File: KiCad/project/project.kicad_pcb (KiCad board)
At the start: 4 copper layers, 50 x 50 mm, 31 parts, among them P1 TerminalBlock 5P 5.0mm, U1 DRV8313PWPR

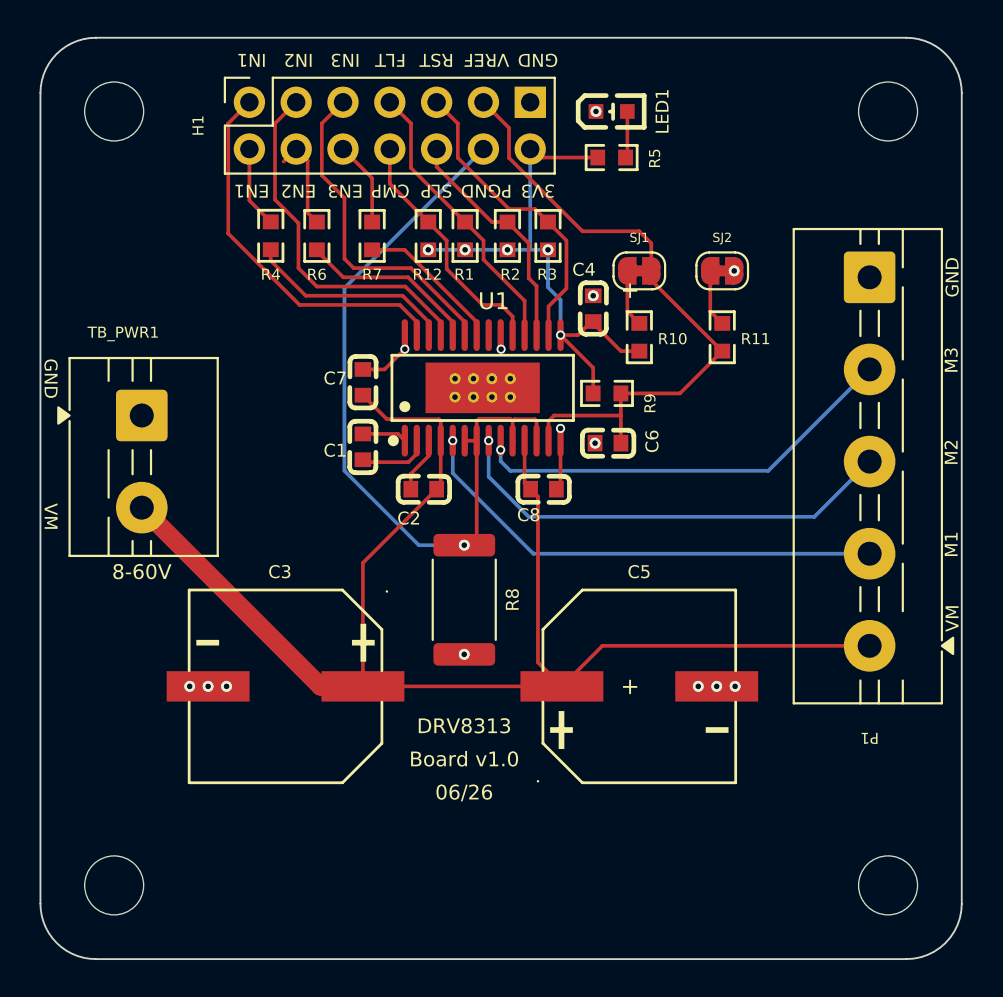
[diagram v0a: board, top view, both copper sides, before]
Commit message: Review manual layout; add power/GND/thermal improvements
Schematic: graphical-only relayout (R8/PGND-label moved, redundant GND
symbol added) — netlist verified byte-identical to prior commit; ERC 101->98.

PCB fixes & improvements:
- Re-ground U1's 8 EP thermal vias (Update-from-Schematic had stripped GND)
  and rename them to pad "29" so they survive every future sync.
- Add Power net class (0.6mm) for VCC/M1/M2/M3/PGND; widen the current-
  carrying runs 0.2->0.6mm with neck-down kept at the HTSSOP escape.
- Add F.Cu + B.Cu GND pours + 38 stitching vias (datasheet 10.1; lowers
  RthJA, better return paths/EMI).
- Extend EP thermal-via array 8->12 (6x2); add GND-return vias at the C7/C8
  VM decoupling caps.

Tooling/docs:
- check_design.py: gate hard on kicad-cli (authoritative for connectivity/
  clearance/shorts); demote KiCadRoutingTools checks to advisory (they false-
  positive on through-pad/off-anchor manual routing); re-baseline ERC to 98.
- Update CLAUDE.md + tools/README.md to match.

Verified: 0 error-severity DRC, 0 unconnected (kicad-cli), check_design PASS.
Manufacturing outputs (manufacturing/, images/) NOT regenerated — still stale.

Co-Authored-By: Claude Opus 4.8 (1M context) <noreply@anthropic.com>
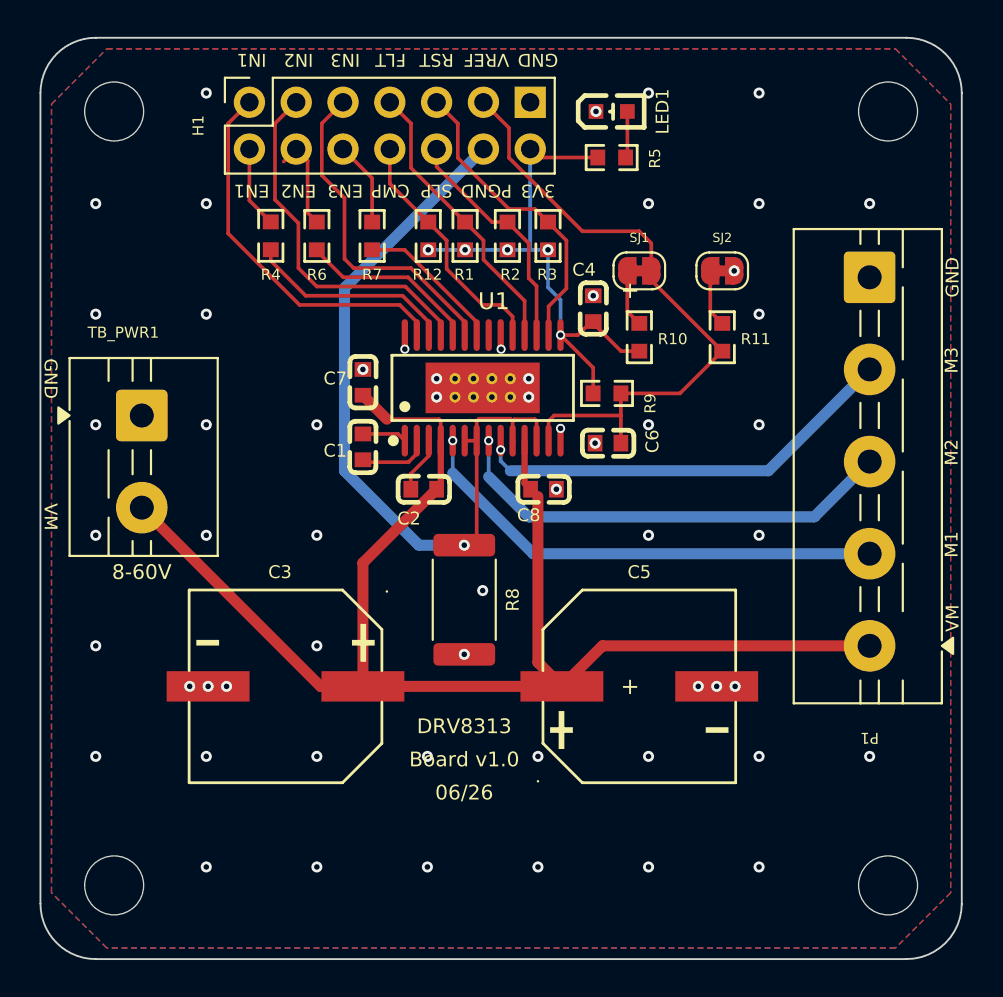
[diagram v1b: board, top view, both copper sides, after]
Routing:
- net GND: track 6.21 -> 1.07 mm, vias 14 -> 58
- added copper zone on B.Cu, net GND
- added copper zone on F.Cu, net GND

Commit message: Enlarge board to 50x50; regenerate fab outputs + square renders
User hand-enlarged the PCB to a full 50x50 mm. Regenerated gerbers, drill,
STEP, and images from the updated board (BOM/CPL unchanged -- no parts moved).

Render canvas was aspect-matched to the old 50x45 board (1600x1440); updated
build_manufacturing.py to 1600x1600 for the now-square board and re-rendered.

Updated CLAUDE.md size references to 50x50 (Goal & status as-built size + dated
note; forward pointer on the superseded 50x45 log entry; render-canvas note).
README spec already updated to 50x50 by the user.

Co-Authored-By: Claude Opus 4.8 (1M context) <noreply@anthropic.com>
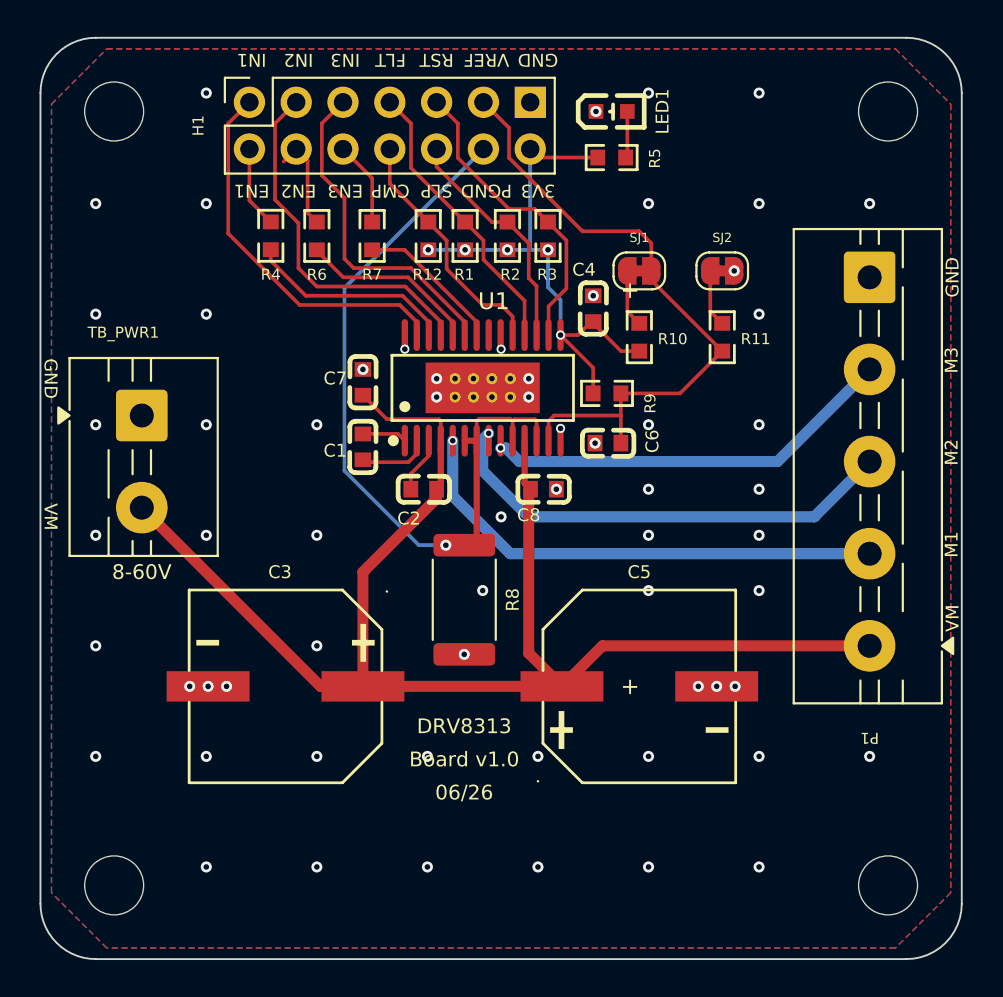
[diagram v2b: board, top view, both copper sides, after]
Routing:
- net M3: track 24.3 -> 22.6 mm
- net PGND: track 42.1 -> 41.1 mm
- net M1: track 27.0 -> 27.7 mm
- net M2: track 24.8 -> 25.4 mm
- net GND: vias 58 -> 63
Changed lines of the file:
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@@
+	)
+	(via
+		(at 173 118)
+		(size 0.6)
+		(drill 0.3)
+		(layers "F.Cu" "B.Cu")
+		(net "GND")
 	)
 	(via
@@
 	)
 	(via
+		(at 159 114)
+		(size 0.6)
+		(drill 0.3)
+		(layers "F.Cu" "B.Cu")
+		(net "GND")
+	)
+	(via
 		(at 173 115)
 		(size 0.6)
@@
 	)
 	(via
+		(at 167 112.5)
+		(size 0.6)
+		(drill 0.3)
+		(layers "F.Cu" "B.Cu")
+		(net "GND")
+	)
+	(via
 		(at 170.7 123.2)
 		(size 0.6)
@@
 	)
 	(via
+		(at 167 118)
+		(size 0.6)
+		(drill 0.3)
+		(layers "F.Cu" "B.Cu")
+		(net "GND")
+	)
+	(via
 		(at 143 115)
 		(size 0.6)
@@
 	(via
 		(at 169.7 123.2)
+		(size 0.6)
+		(drill 0.3)
+		(layers "F.Cu" "B.Cu")
+		(net "GND")
+	)
+	(via
+		(at 173 112.5)
 		(size 0.6)
 		(drill 0.3)
@@
 	)
 	(segment
-		(start 155.5 112.5)
-		(end 151.5 116.5)
-		(width 0.6)
+		(start 160.5 121.4)
+		(end 162.3 123.2)
+		(width 0.6)
+		(layer "F.Cu")
+		(net "VCC")
+	)
+	(segment
+		(start 160.6 112.5)
+		(end 160.2751 112.1751)
+		(width 0.34)
 		(layer "F.Cu")
 		(net "VCC")
@@
 	)
 	(segment
-		(start 161 112.9)
-		(end 161 121.9)
-		(width 0.6)
-		(layer "F.Cu")
-		(net "VCC")
-	)
-	(segment
-		(start 161 121.9)
+		(start 155.5 113)
+		(end 151.5 117)
+		(width 0.6)
+		(layer "F.Cu")
+		(net "VCC")
+	)
+	(segment
+		(start 160.6 112.5)
+		(end 160.5 112.6)
+		(width 0.6)
+		(layer "F.Cu")
+		(net "VCC")
+	)
+	(segment
+		(start 151.5 117)
+		(end 151.5 123.2)
+		(width 0.6)
+		(layer "F.Cu")
+		(net "VCC")
+	)
+	(segment
+		(start 155.5 112.5)
+		(end 155.5 113)
+		(width 0.6)
+		(layer "F.Cu")
+		(net "VCC")
+	)
+	(segment
+		(start 160.5 112.6)
+		(end 160.5 121.4)
+		(width 0.6)
+		(layer "F.Cu")
+		(net "VCC")
+	)
+	(segment
+		(start 164.5 121)
+		(end 179 121)
+		(width 0.6)
+		(layer "F.Cu")
+		(net "VCC")
+	)
+	(segment
+		(start 155.6249 108.70015)
+		(end 155.7249 108.80015)
+		(width 0.2)
+		(layer "F.Cu")
+		(net "VCC")
+	)
+	(segment
+		(start 155.7249 109.8659)
+		(end 155.7249 112.2751)
+		(width 0.34)
+		(layer "F.Cu")
+		(net "VCC")
+	)
+	(segment
+		(start 155.7249 112.2751)
+		(end 155.5 112.5)
+		(width 0.2)
+		(layer "F.Cu")
+		(net "VCC")
+	)
+	(segment
+		(start 162.3 123.2)
+		(end 164.5 121)
+		(width 0.6)
+		(layer "F.Cu")
+		(net "VCC")
+	)
+	(segment
+		(start 160.2751 109.8659)
+		(end 160.3 109.85)
+		(width 0.2)
+		(layer "F.Cu")
+		(net "VCC")
+	)
+	(segment
+		(start 151.5 123.2)
 		(end 162.3 123.2)
 		(width 0.6)
@@
 	)
 	(segment
-		(start 160.6 112.5)
-		(end 160.2751 112.1751)
-		(width 0.34)
-		(layer "F.Cu")
-		(net "VCC")
-	)
-	(segment
-		(start 164.5 121)
-		(end 179 121)
-		(width 0.6)
-		(layer "F.Cu")
-		(net "VCC")
-	)
-	(segment
-		(start 151.5 116.5)
-		(end 151.5 123.2)
-		(width 0.6)
-		(layer "F.Cu")
-		(net "VCC")
-	)
-	(segment
-		(start 155.6249 108.70015)
-		(end 155.7249 108.80015)
-		(width 0.2)
-		(layer "F.Cu")
-		(net "VCC")
-	)
-	(segment
-		(start 155.7249 109.8659)
-		(end 155.7249 112.2751)
-		(width 0.34)
-		(layer "F.Cu")
-		(net "VCC")
-	)
-	(segment
-		(start 155.7249 112.2751)
-		(end 155.5 112.5)
-		(width 0.2)
-		(layer "F.Cu")
-		(net "VCC")
-	)
-	(segment
-		(start 162.3 123.2)
-		(end 164.5 121)
-		(width 0.6)
-		(layer "F.Cu")
-		(net "VCC")
-	)
-	(segment
-		(start 160.6 112.5)
-		(end 161 112.9)
-		(width 0.2)
-		(layer "F.Cu")
-		(net "VCC")
-	)
-	(segment
-		(start 160.2751 109.8659)
-		(end 160.3 109.85)
-		(width 0.2)
-		(layer "F.Cu")
-		(net "VCC")
-	)
-	(segment
-		(start 151.5 123.2)
-		(end 162.3 123.2)
-		(width 0.6)
-		(layer "F.Cu")
-		(net "VCC")
-	)
-	(segment
 		(start 139.5 113.5)
 		(end 149.2 123.2)
@@
 		(start 151.5 107.4)
 		(end 152.80015 108.70015)
-		(width 0.6)
+		(width 0.2)
 		(layer "F.Cu")
 		(net "VCC")
@@
 	)
 	(segment
-		(start 160.7498 116)
+		(start 156.3749 112.8749)
+		(end 159.5 116)
+		(width 0.6)
+		(layer "B.Cu")
+		(net "M1")
+	)
+	(segment
+		(start 159.5 116)
 		(end 179 116)
 		(width 0.6)
@@
 	)
 	(segment
-		(start 156.3749 111.6251)
-		(end 160.7498 116)
+		(start 156.3749 109.8659)
+		(end 156.3749 112.8749)
 		(width 0.6)
 		(layer "B.Cu")
 		(net "M1")
 	)
-	(segment
-		(start 156.3749 109.8659)
-		(end 156.3749 111.6251)
-		(width 0.2)
-		(layer "B.Cu")
-		(net "M1")
-	)
-	(via
-		(at 158.3251 109.8659)
+	(via
+		(at 158.3251 109.4659)
 		(size 0.5)
 		(drill 0.3)
@@
 	)
 	(segment
-		(start 158.3251 109.8659)
-		(end 158.3251 111.8251)
-		(width 0.2)
+		(start 158 111.5)
+		(end 160.5 114)
+		(width 0.6)
+		(layer "B.Cu")
+		(net "M2")
+	)
+	(segment
+		(start 158.3251 109.4659)
+		(end 158 109.791)
+		(width 0.6)
+		(layer "B.Cu")
+		(net "M2")
+	)
+	(segment
+		(start 160.5 114)
+		(end 176 114)
+		(width 0.6)
 		(layer "B.Cu")
 		(net "M2")
@@
 	)
 	(segment
-		(start 160.5 114)
-		(end 176 114)
-		(width 0.6)
-		(layer "B.Cu")
-		(net "M2")
-	)
-	(segment
-		(start 158.3251 111.8251)
-		(end 160.5 114)
+		(start 158 109.791)
+		(end 158 111.5)
 		(width 0.6)
 		(layer "B.Cu")
@@
 	)
 	(via
-		(at 158.9751 110.3659)
+		(at 158.9751 110.2659)
 		(size 0.5)
 		(drill 0.3)
@@
 	)
 	(segment
-		(start 159.5 111.5)
-		(end 173.5 111.5)
+		(start 174 111)
+		(end 179 106)
 		(width 0.6)
 		(layer "B.Cu")
@@
 	)
 	(segment
-		(start 158.9751 109.3659)
-		(end 158.9751 110.9751)
-		(width 0.2)
+		(start 160 111)
+		(end 174 111)
+		(width 0.6)
 		(layer "B.Cu")
 		(net "M3")
 	)
 	(segment
-		(start 173.5 111.5)
-		(end 179 106)
+		(start 158.9751 110.2659)
+		(end 159.2659 110.2659)
 		(width 0.6)
 		(layer "B.Cu")
@@
 	)
 	(segment
-		(start 158.9751 110.9751)
-		(end 159.5 111.5)
-		(width 0.2)
+		(start 159.2659 110.2659)
+		(end 160 111)
+		(width 0.6)
 		(layer "B.Cu")
 		(net "M3")
@@
 		(start 157.6751 109.8659)
 		(end 157.6751 115.2126)
-		(width 0.2)
+		(width 0.34)
 		(layer "F.Cu")
 		(net "PGND")
@@
 		(start 157.0249 109.8659)
 		(end 157.6751 109.8659)
-		(width 0.2)
+		(width 0.34)
 		(layer "F.Cu")
 		(net "PGND")
@@
 	)
 	(via
-		(at 157 115.5375)
-		(size 0.6)
-		(drill 0.3)
-		(layers "F.Cu" "B.Cu")
+		(at 156 115.5375)
+		(size 0.6)
+		(drill 0.3)
+		(layers "F.Cu" "B.Cu")
+		(net "PGND")
+	)
+	(segment
+		(start 156 115.5375)
+		(end 154.5375 115.5375)
+		(width 0.2)
+		(layer "B.Cu")
+		(net "PGND")
+	)
+	(segment
+		(start 150.5 101.58)
+		(end 158.04 94.04)
+		(width 0.2)
+		(layer "B.Cu")
+		(net "PGND")
+	)
+	(segment
+		(start 154.5375 115.5375)
+		(end 150.5 111.5)
+		(width 0.2)
+		(layer "B.Cu")
 		(net "PGND")
 	)
@@
 		(start 150.5 111.5)
 		(end 150.5 101.58)
-		(width 0.6)
-		(layer "B.Cu")
-		(net "PGND")
-	)
-	(segment
-		(start 154.5375 115.5375)
-		(end 150.5 111.5)
-		(width 0.6)
-		(layer "B.Cu")
-		(net "PGND")
-	)
-	(segment
-		(start 157 115.5375)
-		(end 154.5375 115.5375)
-		(width 0.6)
-		(layer "B.Cu")
-		(net "PGND")
-	)
-	(segment
-		(start 150.5 101.58)
-		(end 158.04 94.04)
-		(width 0.6)
-		(layer "B.Cu")
-		(net "PGND")
+		(width 0.2)
+		(layer "B.Cu")
+		(net "PGND")

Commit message: Rename project library simplefocmini -> drv8313-board
The board long ago diverged from SimpleFOCMini, so renamed the project KiCad
library nickname (used for both the footprint .pretty and the symbol .kicad_sym)
to match the repo/manufacturing naming.

- Renamed KiCad/project/simplefocmini.pretty -> drv8313-board.pretty and
  simplefocmini.kicad_sym -> drv8313-board.kicad_sym (git mv).
- Updated the project fp-lib-table + sym-lib-table (name + URI), all PCB FPIDs
  (21) and schematic lib_ids/Footprint fields (25), and the BOM Footprint column.
- Updated the lib-name references in README/CLAUDE.md; preserved the legitimate
  SimpleFOCMini attribution, the EasyEDA source URL, and the historical Altium
  filename.

Footprints + symbols re-verified to resolve under the new nickname (parity found
the lib; ERC 0). check_design.py PASS (DRC 0 errors, ERC 0). Netlist/PCB
geometry unchanged; project.kicad_pro untouched.

Co-Authored-By: Claude Opus 4.8 (1M context) <noreply@anthropic.com>
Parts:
- C1, C2, C4, C6, C7, C8: footprint simplefocmini:C0603 -> drv8313-board:C0603
- C3, C5: footprint simplefocmini:CAP-SMD_BD10.0-L10.3-W10.3-FD-LS11.0 -> drv8313-board:CAP-SMD_BD10.0-L10.3-W10.3-FD-LS11.0
- LED1: footprint simplefocmini:LED0603-R-RD -> drv8313-board:LED0603-R-RD
- R1, R10, R11, R12, R2, R3, R4, R5, R6, R7, R9: footprint simplefocmini:R0603 -> drv8313-board:R0603
- U1: footprint simplefocmini:HTSSOP-28_L9.8-W4.5-P0.65-LS6.6-BL-EP -> drv8313-board:HTSSOP-28_L9.8-W4.5-P0.65-LS6.6-BL-EP
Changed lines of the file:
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@@
 		)
 	)
-	(footprint "simplefocmini:C0603"
+	(footprint "drv8313-board:C0603"
 		(layer "F.Cu")
 		(at 164.8 110 180)
@@
 		)
 	)
-	(footprint "simplefocmini:R0603"
+	(footprint "drv8313-board:R0603"
 		(layer "F.Cu")
 		(at 165 94.5)
@@
 		(embedded_fonts no)
 	)
-	(footprint "simplefocmini:C0603"
+	(footprint "drv8313-board:C0603"
 		(layer "F.Cu")
 		(at 154.8 112.5 180)
@@
 		(embedded_fonts no)
 	)
-	(footprint "simplefocmini:R0603"
+	(footprint "drv8313-board:R0603"
 		(layer "F.Cu")
 		(at 155.045 98.7534 -90)
@@
 		)
 	)
-	(footprint "simplefocmini:R0603"
+	(footprint "drv8313-board:R0603"
 		(layer "F.Cu")
 		(at 164.7466 107.3)
@@
 		)
 	)
-	(footprint "simplefocmini:HTSSOP-28_L9.8-W4.5-P0.65-LS6.6-BL-EP"
+	(footprint "drv8313-board:HTSSOP-28_L9.8-W4.5-P0.65-LS6.6-BL-EP"
 		(locked yes)
 		(layer "F.Cu")
@@
 		(embedded_fonts no)
 	)
-	(footprint "simplefocmini:R0603"
+	(footprint "drv8313-board:R0603"
 		(layer "F.Cu")
 		(at 161.545 98.7534 90)
@@
 		)
 	)
-	(footprint "simplefocmini:R0603"
+	(footprint "drv8313-board:R0603"
 		(layer "F.Cu")
 		(at 152 98.7534 -90)
@@
 		)
 	)
-	(footprint "simplefocmini:R0603"
+	(footprint "drv8313-board:R0603"
 		(layer "F.Cu")
 		(at 149 98.7534 -90)
@@
 		)
 	)
-	(footprint "simplefocmini:R0603"
+	(footprint "drv8313-board:R0603"
 		(layer "F.Cu")
 		(at 159.345 98.7534 90)
@@
 		)
 	)
-	(footprint "simplefocmini:CAP-SMD_BD10.0-L10.3-W10.3-FD-LS11.0"
+	(footprint "drv8313-board:CAP-SMD_BD10.0-L10.3-W10.3-FD-LS11.0"
 		(layer "F.Cu")
 		(at 166.5 123.2)
@@
 		)
 	)
-	(footprint "simplefocmini:C0603"
+	(footprint "drv8313-board:C0603"
 		(layer "F.Cu")
 		(at 151.5 106.7 -90)
@@
 		)
 	)
-	(footprint "simplefocmini:R0603"
+	(footprint "drv8313-board:R0603"
 		(layer "F.Cu")
 		(at 157.045 98.7534 90)
@@
 		)
 	)
-	(footprint "simplefocmini:R0603"
+	(footprint "drv8313-board:R0603"
 		(layer "F.Cu")
 		(at 166.5 104.2534 90)
@@
 		)
 	)
-	(footprint "simplefocmini:C0603"
+	(footprint "drv8313-board:C0603"
 		(layer "F.Cu")
 		(at 161.3 112.5 180)
@@
 		)
 	)
-	(footprint "simplefocmini:R0603"
+	(footprint "drv8313-board:R0603"
 		(layer "F.Cu")
 		(at 171 104.2534 90)
@@
 		)
 	)
-	(footprint "simplefocmini:R0603"
+	(footprint "drv8313-board:R0603"
 		(layer "F.Cu")
 		(at 146.5 98.7466 -90)
@@
 		(embedded_fonts no)
 	)
-	(footprint "simplefocmini:LED0603-R-RD"
+	(footprint "drv8313-board:LED0603-R-RD"
 		(layer "F.Cu")
 		(at 165 92)
@@
 		)
 	)
-	(footprint "simplefocmini:C0603"
+	(footprint "drv8313-board:C0603"
 		(layer "F.Cu")
 		(at 151.5 110.2 90)
@@
 		)
 	)
-	(footprint "simplefocmini:C0603"
+	(footprint "drv8313-board:C0603"
 		(layer "F.Cu")
 		(at 164 102.7 -90)
@@
 		)
 	)
-	(footprint "simplefocmini:CAP-SMD_BD10.0-L10.3-W10.3-FD-LS11.0"
+	(footprint "drv8313-board:CAP-SMD_BD10.0-L10.3-W10.3-FD-LS11.0"
 		(layer "F.Cu")
 		(at 147.3 123.2 180)
